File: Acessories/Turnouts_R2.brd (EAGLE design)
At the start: 160 x 100 mm, 197 parts, among them IC1 MCP23008/P, IC2 LTC485S, IC4 MCP23008/P, J1 AVR_SPI_PROG_3X2NS, J3 4P-2.0, J4 RJ11, J5 RJ11, J6 RJ11, J7 RJ11, M1 XL6009, Q1 BD679, Q10 BD679, Q11 BD679, Q12 BD679, Q13 BD679, Q14 BD679, Q15 BD679, Q16 BD679, Q17 BSS123, Q18 BD679, Q2 BD679, Q3 BD679, Q4 BD679, Q5 BD679, Q6 BD679, Q7 BD679, Q8 BD679, Q9 BD679, T1 BC847, U3 ATMEGA1284P, X1 MKDSN1,5/4-5,08, X10 1751303, X2 1751280, X3 1751280, X4 1751248, X5 1751280, X6 1751280, X7 1751303, X8 1751303, X9 1751303, Y1 HC49UP

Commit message: Add files via upload
Added learn switch, modified the CDU and  2 x 8 distribution strip for DCC to sections
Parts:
- removed LED20: Amber, adafruit:LED3MM
- removed M1: XL6009, GJR:XL6009
- removed R58: 3K3, rcl:R0805
- removed X4: 1751248, con-phoenix-350:1751248
- added S1: (no value), adafruit:EG1218
- added X11: MKKDS1/8-3,5, con-phoenix-350:MKKDS1/8-3,5
- D24, D26: value MBRS340T3 -> (none); device diode:SMC -> diode:SMB
- R8: value 0.22R -> 10K; device rcl:R2512 -> rcl:R0805
- moved R8 60.6 mm to (66.2, 41.5)
- moved LED23 26.2 mm to (119.2, 41.8)
- moved R73 26.2 mm to (119.2, 37.8)
- moved C14 20.3 mm to (123.8, 70.2)
- moved C16 20.0 mm to (141.8, 70.5)
- moved D26 19.6 mm to (132.0, 62.8)
- moved C13 19.5 mm to (123.8, 52.5)
- moved C15 19.3 mm to (141.5, 52.8)
- moved D25 14.3 mm to (155.0, 47.5)
- moved Q18 14.3 mm to (156.2, 40.5)
- moved R68 14.3 mm to (139.2, 32.0)
- moved R71 14.3 mm to (142.5, 37.8)
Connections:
- removed net +18V: LED23.A, M1.OUT+, R68.1, R71.2
- removed net N$35: LED20.K, R58.2
- removed net OC1-2: Q1.E, Q3.E, R8.2, U3.33
- new net LEARN: R8.1, S1.P, U3.33
- net +15V: now also R68.1, R71.2; no longer M1.IN+
- net +5V: now also R8.2
- net CDU: now also LED23.A; no longer LED20.A
- net GND: now also Q1.E, Q3.E, S1.S; no longer M1.IN-, M1.OUT-, R58.1, R8.1
- net T1F: now also X11.1, X11.11, X11.13, X11.15, X11.3, X11.5, X11.7, X11.9; no longer X4.1
- net TRACK2: now also X11.10, X11.12, X11.14, X11.16, X11.2, X11.4, X11.6, X11.8; no longer X4.2
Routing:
- net OC1-2: track 100.7 -> 0.00 mm, vias 1 -> 0
- net +18V: track 55.2 -> 0.00 mm
- net LEARN: track 0.00 -> 26.4 mm, vias 0 -> 1
- net T1F: track 129.8 -> 116.5 mm, vias 3 -> 2
- net +21V: track 376.7 -> 389.2 mm
- net GND: track 2.86 -> 9.86 mm
- net CDU: track 117.7 -> 122.2 mm
- net +15V: track 72.8 -> 68.3 mm, vias 1 -> 0
- net +5V: track 291.5 -> 295.3 mm
- net TRACK2: track 184.2 -> 187.8 mm, vias 2 -> 1
- net N$35: track 2.53 -> 0.00 mm
- net N$1: track 8.20 -> 10.1 mm
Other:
- board text added: "DCC Accessory Board Rev 1.5 May 2019"
- board text added: "Learn"
- board text removed: "DCC Accessory Board Rev 1.4 November 2018"

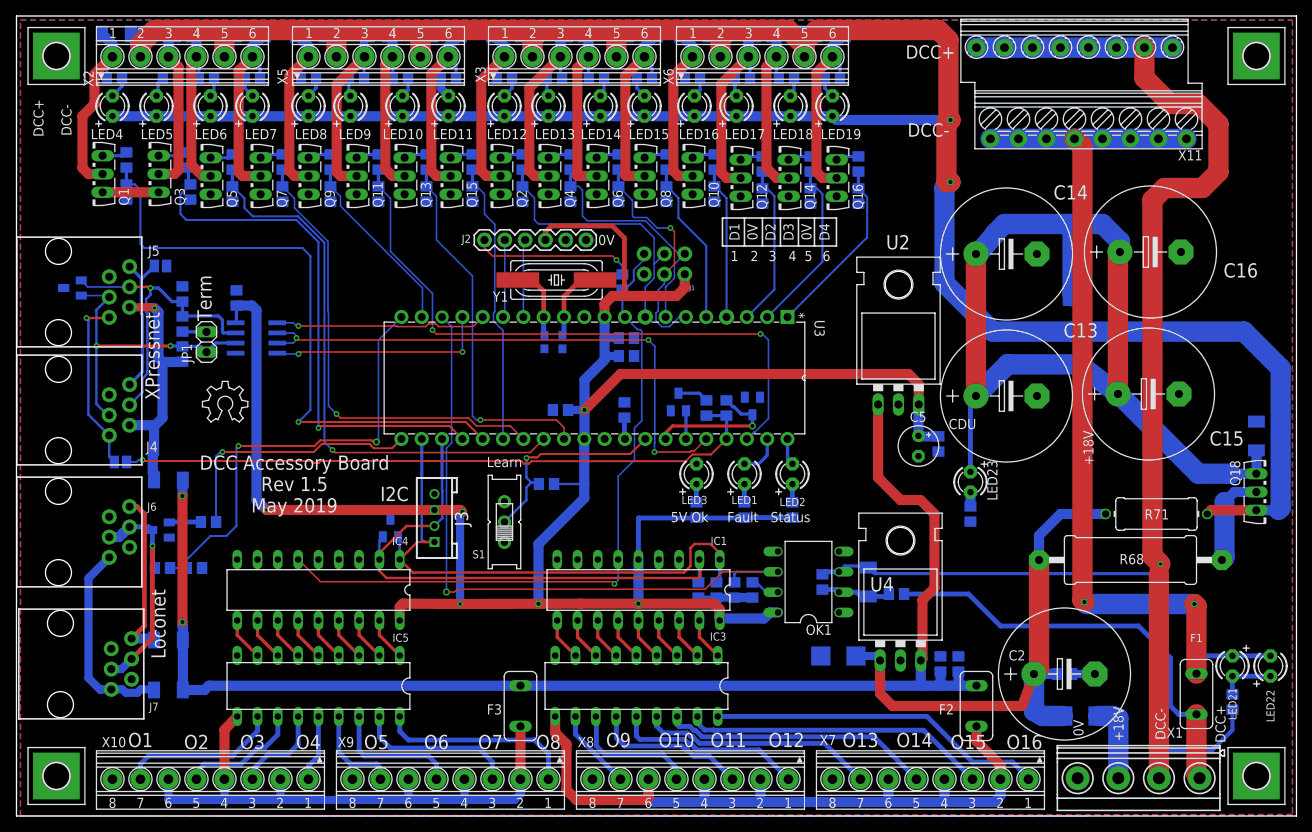
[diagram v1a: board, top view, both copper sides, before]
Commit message: Add files via upload
Added Turntable board based on Nano
Added learn switch to Turnouts board, moved parts to allow for DC/DC modules
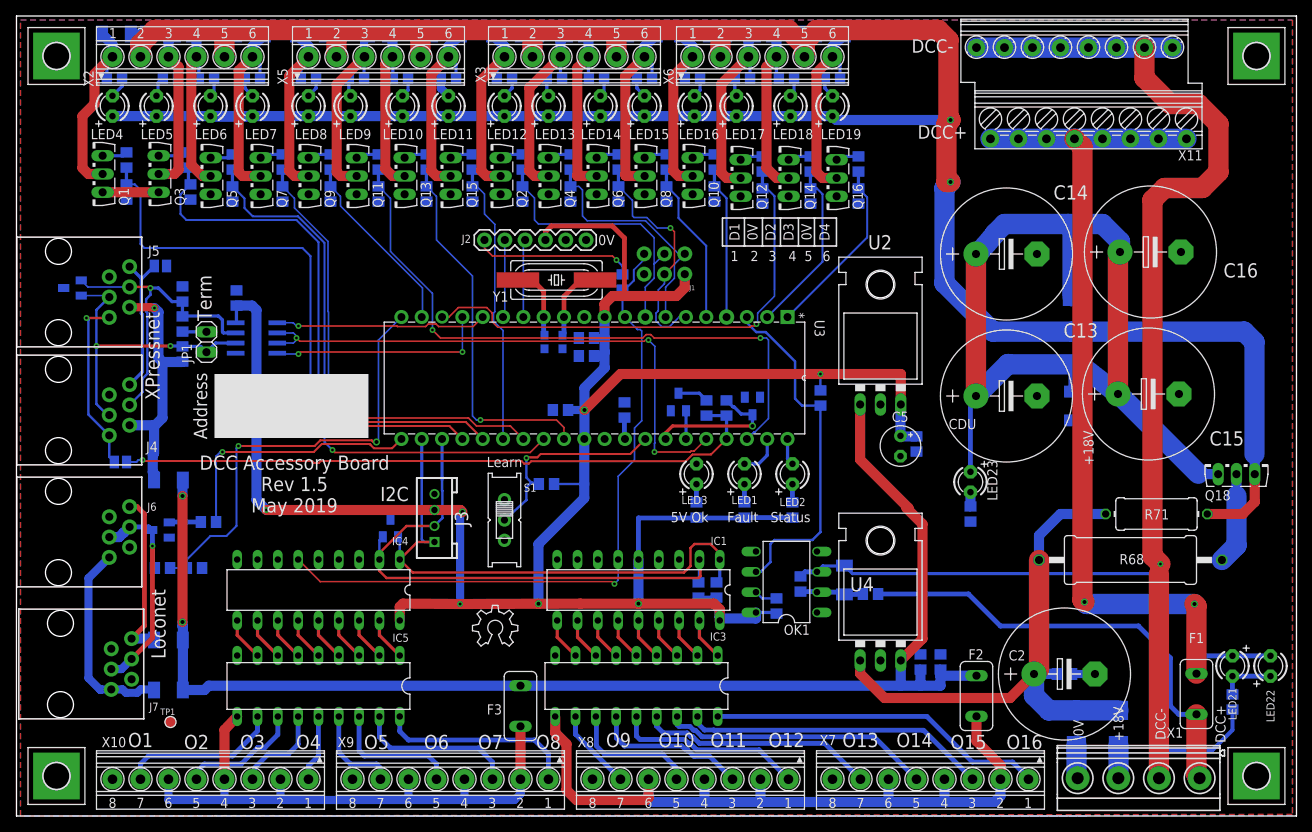
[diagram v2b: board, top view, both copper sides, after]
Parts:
- added TP1: (no value), RCLDT:TP-1.5RUND
- moved LOGO1 43.9 mm to (57.0, 21.2)
- moved Z1 31.1 mm to (132.5, 11.0), turned to 270 degrees
- moved R14 26.3 mm to (100.5, 52.2), turned to 90 degrees
- moved D25 23.3 mm to (132.0, 51.2), turned to 270 degrees
- moved Q18 5.13 mm to (152.5, 44.0), turned to 0 degrees
- moved C10 5.00 mm to (71.2, 57.5), turned to 0 degrees
- moved C9 5.00 mm to (71.2, 59.8), turned to 0 degrees
- moved D24 4.98 mm to (137.8, 11.0), turned to 270 degrees
- moved R11 3.61 mm to (95.0, 26.2)
- moved R4 3.25 mm to (106.8, 27.8)
- moved D1 3.01 mm to (103.5, 29.5)
- moved C1 2.76 mm to (98.0, 29.0)
- moved C4 2.75 mm to (112.5, 46.5)
- moved OK1 2.75 mm to (96.2, 29.2)
- moved C18 2.51 mm to (113.0, 19.2)
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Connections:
- net DCCIN: now also U3.3; no longer U3.18
- net ENT7B: now also U3.18; no longer U3.3
- net GND: now also S1.O, TP1.1; no longer S1.S
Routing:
- net ENT7B: track 20.6 -> 62.6 mm, vias 0 -> 1
- net DCCIN: track 84.2 -> 44.2 mm, vias 1 -> 0
- net +5V: track 295.3 -> 288.1 mm, vias 6 -> 7
- net N$1: track 10.1 -> 4.08 mm
- net +21V: track 389.2 -> 384.1 mm
- net CDU: track 122.2 -> 117.7 mm
- net GND: track 9.86 -> 14.0 mm
- net TRACK1: track 54.4 -> 57.7 mm
- net TRACK2: track 187.8 -> 190.6 mm
- net +15V: track 68.3 -> 69.8 mm
- net N$29: track 91.3 -> 92.6 mm
- net N$4: track 3.70 -> 2.88 mm
- net N$2: track 8.78 -> 7.97 mm
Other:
- board text added: "Address"

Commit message: Add files via upload
Changed Diodes on Turnouts board to SMP
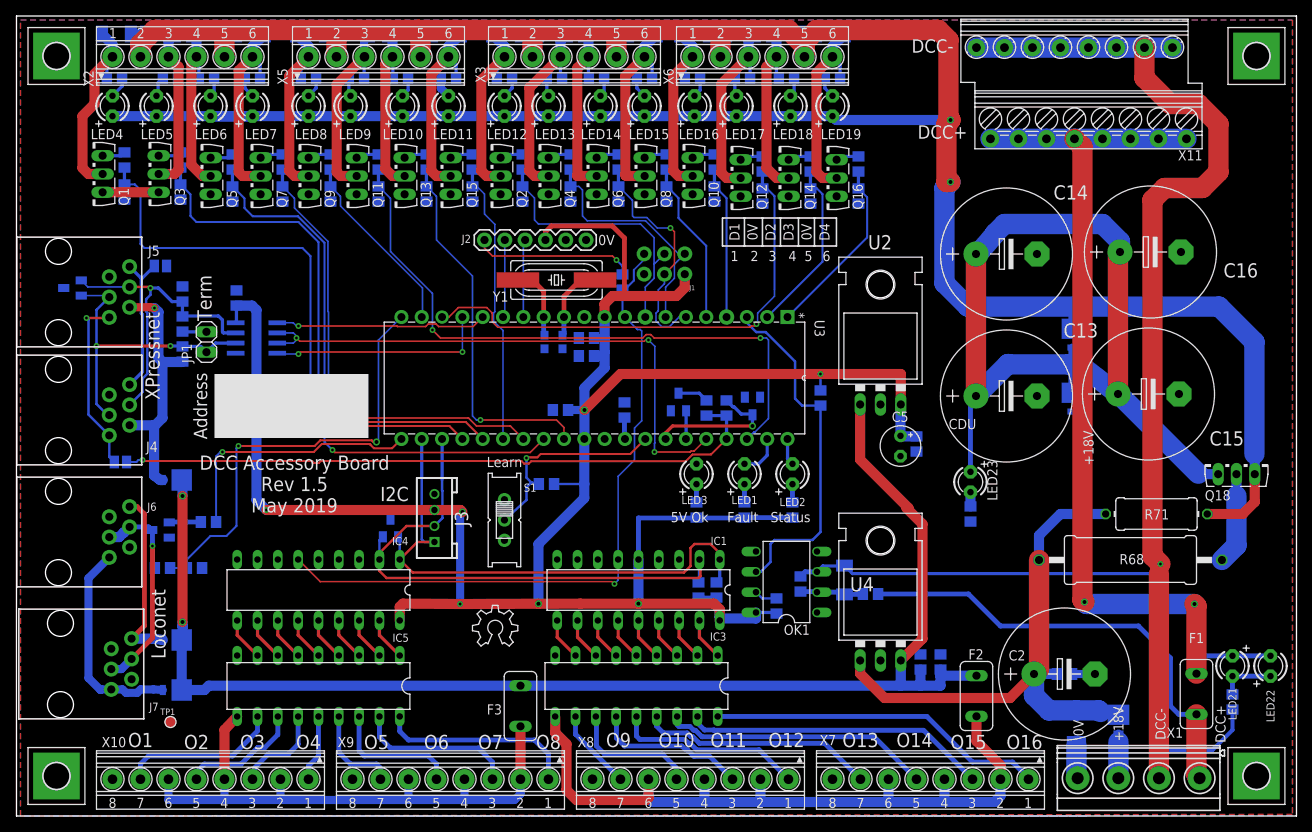
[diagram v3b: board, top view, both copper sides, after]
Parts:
- D21, D22, D23, D25: value CGRM4002-G -> MICROSMD-SCHOTTKY-DIODESMP; device diode:SOD-123_MINI-SMA -> GJR:SMP
- D24, D26: value (none) -> MICROSMD-SCHOTTKY-DIODESMP; device diode:SMB -> GJR:SMP
- moved D26 3.50 mm to (132.0, 59.2), turned to 270 degrees
- moved R12 1.25 mm to (20.5, 78.0)
- moved R9 1.00 mm to (20.5, 82.0)
- moved R2 0.25 mm to (13.5, 78.0)
- moved R6 0.25 mm to (13.5, 82.0)
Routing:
- net CDU: track 117.7 -> 110.9 mm
- net +21V: track 384.1 -> 387.0 mm
- net N$1: track 4.08 -> 5.58 mm
- net ENT1B: track 67.1 -> 65.9 mm
- net N$51: track 25.4 -> 26.5 mm
- net N$27: track 21.4 -> 22.4 mm
- net N$40: track 3.90 -> 2.90 mm
- net +15V: track 69.8 -> 70.6 mm
- net XP_12V: track 31.3 -> 31.9 mm
